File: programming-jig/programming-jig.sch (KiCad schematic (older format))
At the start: 9 parts, among them J1 854-22-005-10-001101, J2 854-22-005-10-001101, J3 825-22-002-10-001101, J4 CONN_02X05, J5 USB_C_Receptacle

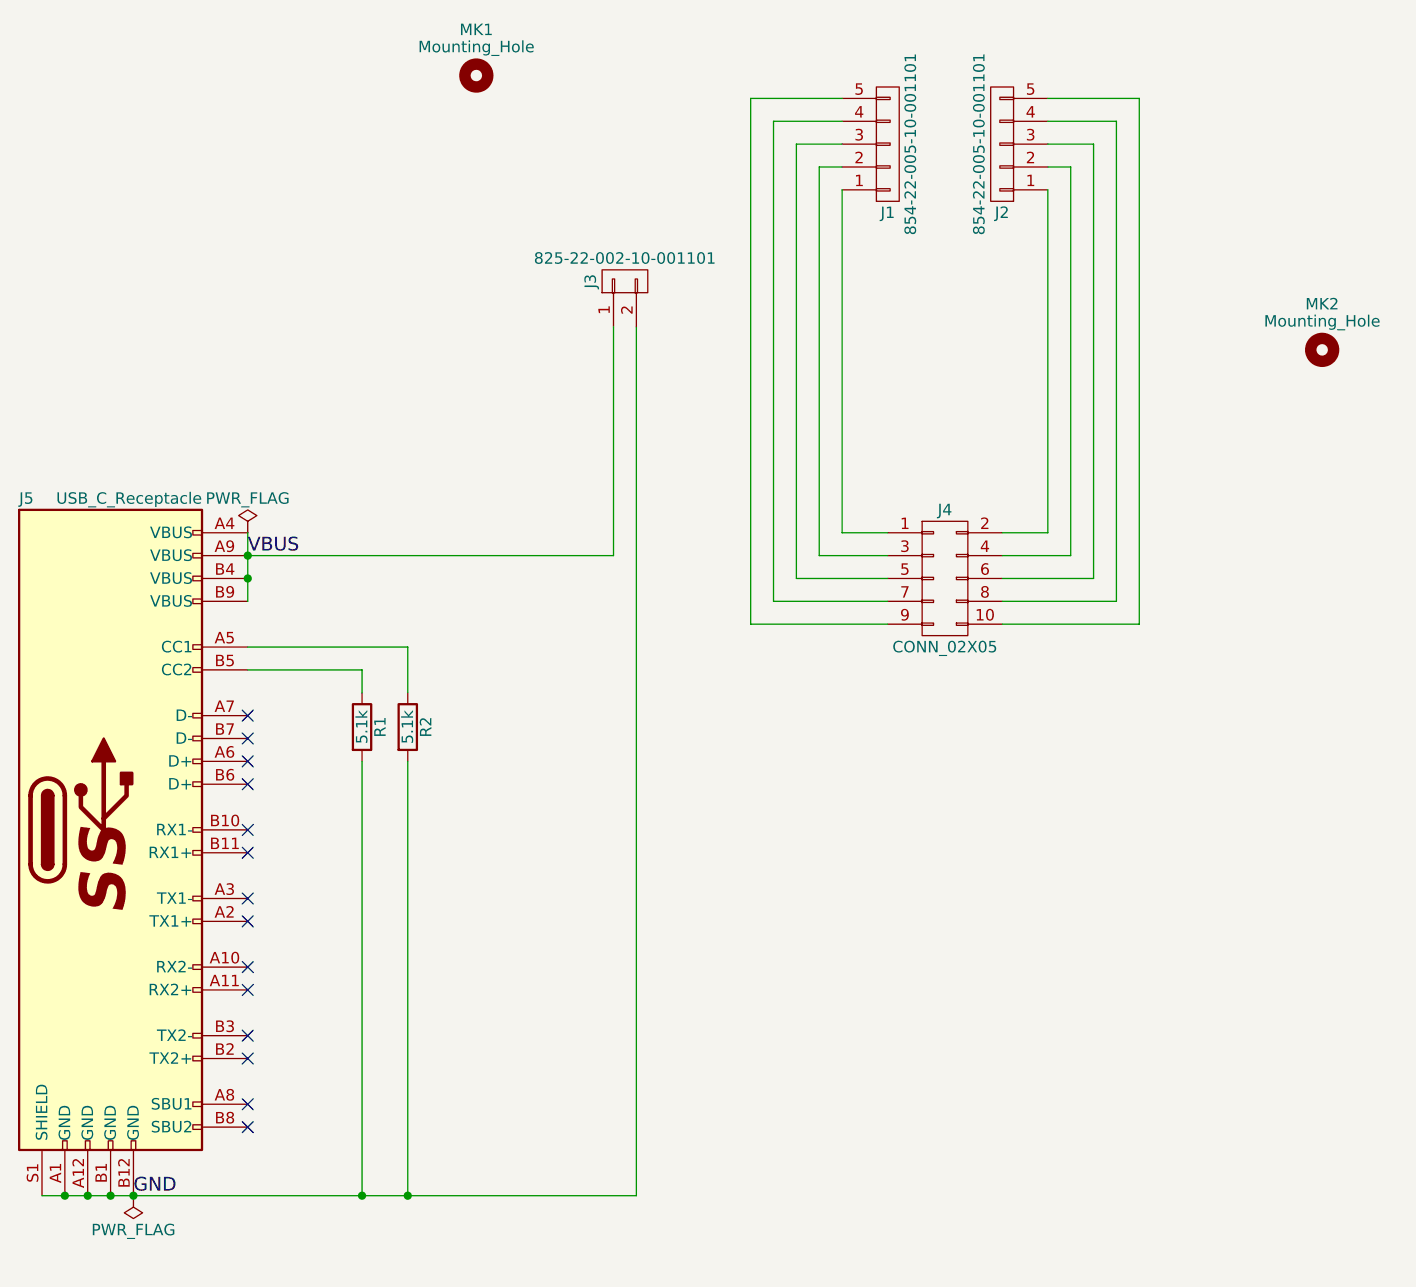
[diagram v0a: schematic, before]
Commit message: Use power symbols in programming jig schematic
The power lines had been drawn as regular wires with net labels.  That's
not great, so I changed them to use power symbols.  It's better now!
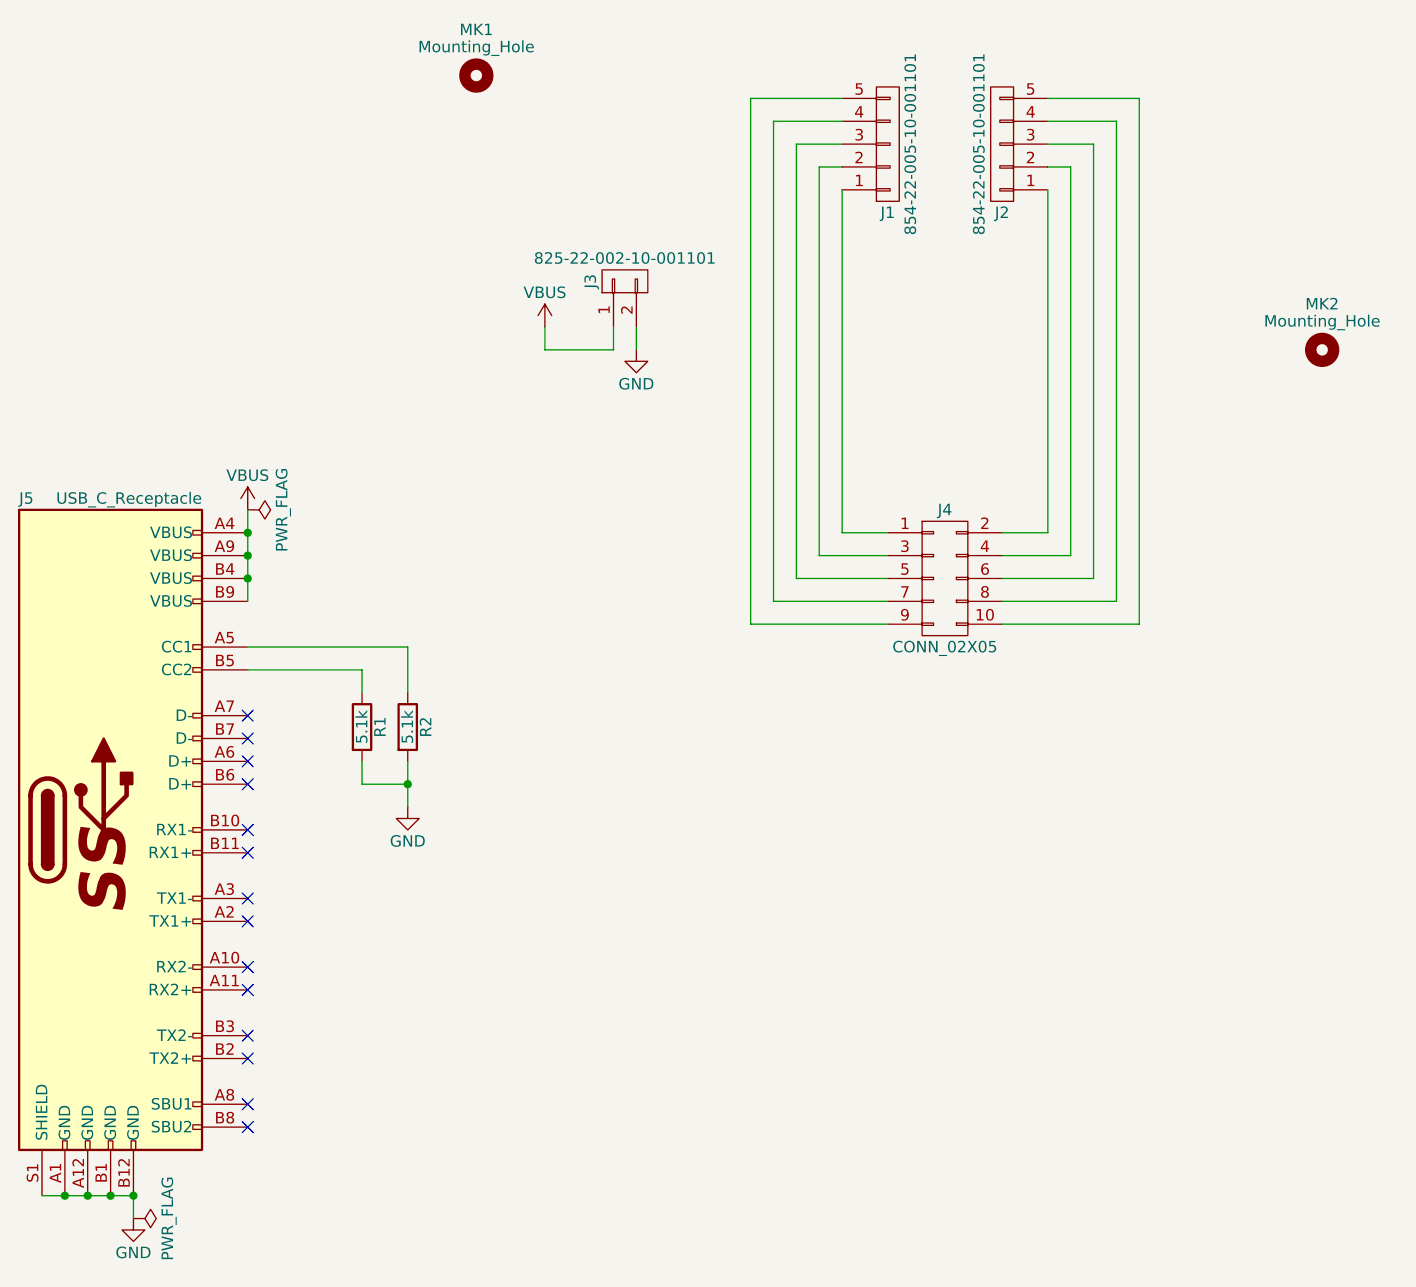
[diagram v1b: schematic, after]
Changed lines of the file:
@@
 Connection ~ 2200 5700
 Wire Wire Line
-	2800 2800 2800 2900
-Wire Wire Line
-	2800 2900 2800 3000
-Wire Wire Line
-	2800 3000 2800 3100
+	2800 2700 2800 3100
 Connection ~ 2800 3000
 Connection ~ 2800 2900
@@
 L PWR_FLAG #FLG01
 U 1 1 5917BAD1
-P 2800 2800
-F 0 "#FLG01" H 2800 2875 50  0001 C CNN
-F 1 "PWR_FLAG" H 2800 2950 50  0000 C CNN
-F 2 "" H 2800 2800 50  0001 C CNN
-F 3 "" H 2800 2800 50  0001 C CNN
-	1    2800 2800
-	1    0    0    -1
+P 2800 2700
+F 0 "#FLG01" H 2800 2775 50  0001 C CNN
+F 1 "PWR_FLAG" H 2800 2850 50  0000 C CNN
+F 2 "" H 2800 2700 50  0001 C CNN
+F 3 "" H 2800 2700 50  0001 C CNN
+	1    2800 2700
+	0    1    1    0
 $EndComp
 $Comp
 L PWR_FLAG #FLG02
 U 1 1 5917BAFB
-P 2300 5700
-F 0 "#FLG02" H 2300 5775 50  0001 C CNN
-F 1 "PWR_FLAG" H 2300 5850 50  0000 C CNN
-F 2 "" H 2300 5700 50  0001 C CNN
-F 3 "" H 2300 5700 50  0001 C CNN
-	1    2300 5700
-	-1   0    0    1
+P 2300 5800
+F 0 "#FLG02" H 2300 5875 50  0001 C CNN
+F 1 "PWR_FLAG" H 2300 5950 50  0000 C CNN
+F 2 "" H 2300 5800 50  0001 C CNN
+F 3 "" H 2300 5800 50  0001 C CNN
+	1    2300 5800
+	0    1    1    0
 $EndComp
-Text Label 2800 2900 0    60   ~ 0
-VBUS
-Text Label 2300 5700 0    60   ~ 0
-GND
 NoConn ~ 2800 3900
 NoConn ~ 2800 3800
 NoConn ~ 2800 3700
 NoConn ~ 2800 3600
-Wire Wire Line
-	1900 5700 2000 5700
-Wire Wire Line
-	2000 5700 2100 5700
-Wire Wire Line
-	2100 5700 2200 5700
-Wire Wire Line
-	2200 5700 2300 5700
-Wire Wire Line
-	2300 5700 3300 5700
-Wire Wire Line
-	3300 5700 3500 5700
-Wire Wire Line
-	3500 5700 4500 5700
-Wire Wire Line
-	4500 5700 4500 1900
 Connection ~ 2300 5700
-Wire Wire Line
-	4400 1900 4400 2900
-Wire Wire Line
-	4400 2900 2800 2900
 $Comp
 L R R1
@@
 Wire Wire Line
 	3300 3400 3300 3500
+Connection ~ 2800 2800
+$Comp
+L VBUS #PWR?
+U 1 1 592B59CF
+P 2800 2700
+F 0 "#PWR?" H 2800 2550 50  0001 C CNN
+F 1 "VBUS" H 2800 2850 50  0000 C CNN
+F 2 "" H 2800 2700 50  0001 C CNN
+F 3 "" H 2800 2700 50  0001 C CNN
+	1    2800 2700
+	1    0    0    -1
+$EndComp
 Wire Wire Line
-	3300 3800 3300 5700
-Connection ~ 3300 5700
+	1900 5700 2300 5700
 Wire Wire Line
-	3500 3800 3500 5700
-Connection ~ 3500 5700
+	2300 5700 2300 5800
+$Comp
+L GND #PWR?
+U 1 1 592B5BC0
+P 2300 5800
+F 0 "#PWR?" H 2300 5550 50  0001 C CNN
+F 1 "GND" H 2300 5650 50  0000 C CNN
+F 2 "" H 2300 5800 50  0001 C CNN
+F 3 "" H 2300 5800 50  0001 C CNN
+	1    2300 5800
+	1    0    0    -1
+$EndComp
+$Comp
+L GND #PWR?
+U 1 1 592B5F56
+P 3500 4000
+F 0 "#PWR?" H 3500 3750 50  0001 C CNN
+F 1 "GND" H 3500 3850 50  0000 C CNN
+F 2 "" H 3500 4000 50  0001 C CNN
+F 3 "" H 3500 4000 50  0001 C CNN
+	1    3500 4000
+	1    0    0    -1
+$EndComp
+Wire Wire Line
+	3500 3800 3500 4000
+Wire Wire Line
+	3300 3800 3300 3900
+Wire Wire Line
+	3300 3900 3500 3900
+Connection ~ 3500 3900
+Wire Wire Line
+	4400 1900 4400 2000
+Wire Wire Line
+	4400 2000 4100 2000
+Wire Wire Line
+	4100 2000 4100 1900
+Wire Wire Line
+	4500 1900 4500 2000
+$Comp
+L GND #PWR?
+U 1 1 592B68D9
+P 4500 2000
+F 0 "#PWR?" H 4500 1750 50  0001 C CNN
+F 1 "GND" H 4500 1850 50  0000 C CNN
+F 2 "" H 4500 2000 50  0001 C CNN
+F 3 "" H 4500 2000 50  0001 C CNN
+	1    4500 2000
+	1    0    0    -1
+$EndComp
+$Comp
+L VBUS #PWR?
+U 1 1 592B68FF
+P 4100 1900
+F 0 "#PWR?" H 4100 1750 50  0001 C CNN
+F 1 "VBUS" H 4100 2050 50  0000 C CNN
+F 2 "" H 4100 1900 50  0001 C CNN
+F 3 "" H 4100 1900 50  0001 C CNN
+	1    4100 1900
+	1    0    0    -1
+$EndComp
 $EndSCHEMATC

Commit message: Use USB connector footprints from KiCad library
No need to provide our own anymore now that they're all merged upstream.
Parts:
- J5: footprint pd-buddy:Amphenol-12401548E4#2A -> Connectors_USB:USB_C_Receptacle_Amphenol_12401548E4-2A_CircularHoles
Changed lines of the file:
@@
 F 0 "J5" H 1800 5550 50  0000 L CNN
 F 1 "USB_C_Receptacle" H 2600 5550 50  0000 R CNN
-F 2 "pd-buddy:Amphenol-12401548E4#2A" H 2350 4100 50  0001 C CNN
+F 2 "Connectors_USB:USB_C_Receptacle_Amphenol_12401548E4-2A_CircularHoles" H 2350 4100 50  0001 C CNN
 F 3 "" H 2350 4100 50  0001 C CNN
 	1    2200 4100
@@
 Connection ~ 2800 2800
 $Comp
-L VBUS #PWR?
+L VBUS #PWR03
 U 1 1 592B59CF
 P 2800 2700
-F 0 "#PWR?" H 2800 2550 50  0001 C CNN
+F 0 "#PWR03" H 2800 2550 50  0001 C CNN
 F 1 "VBUS" H 2800 2850 50  0000 C CNN
 F 2 "" H 2800 2700 50  0001 C CNN
@@
 	2300 5700 2300 5800
 $Comp
-L GND #PWR?
+L GND #PWR04
 U 1 1 592B5BC0
 P 2300 5800
-F 0 "#PWR?" H 2300 5550 50  0001 C CNN
+F 0 "#PWR04" H 2300 5550 50  0001 C CNN
 F 1 "GND" H 2300 5650 50  0000 C CNN
 F 2 "" H 2300 5800 50  0001 C CNN
@@
 $EndComp
 $Comp
-L GND #PWR?
+L GND #PWR05
 U 1 1 592B5F56
 P 3500 4000
-F 0 "#PWR?" H 3500 3750 50  0001 C CNN
+F 0 "#PWR05" H 3500 3750 50  0001 C CNN
 F 1 "GND" H 3500 3850 50  0000 C CNN
 F 2 "" H 3500 4000 50  0001 C CNN
@@
 	4500 1900 4500 2000
 $Comp
-L GND #PWR?
+L GND #PWR06
 U 1 1 592B68D9
 P 4500 2000
-F 0 "#PWR?" H 4500 1750 50  0001 C CNN
+F 0 "#PWR06" H 4500 1750 50  0001 C CNN
 F 1 "GND" H 4500 1850 50  0000 C CNN
 F 2 "" H 4500 2000 50  0001 C CNN
@@
 $EndComp
 $Comp
-L VBUS #PWR?
+L VBUS #PWR07
 U 1 1 592B68FF
 P 4100 1900
-F 0 "#PWR?" H 4100 1750 50  0001 C CNN
+F 0 "#PWR07" H 4100 1750 50  0001 C CNN
 F 1 "VBUS" H 4100 2050 50  0000 C CNN
 F 2 "" H 4100 1900 50  0001 C CNN
